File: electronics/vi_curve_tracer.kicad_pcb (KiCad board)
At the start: 2 copper layers, 60 x 37 mm, 65 parts, among them P1 CONN_01X05, P2 USB_OTG, P3 CONN_01X06, P4 CONN_01X06, P5 CONN_01X02, U1 MCP6004, U2 pic24f08km202, U3 ft230x

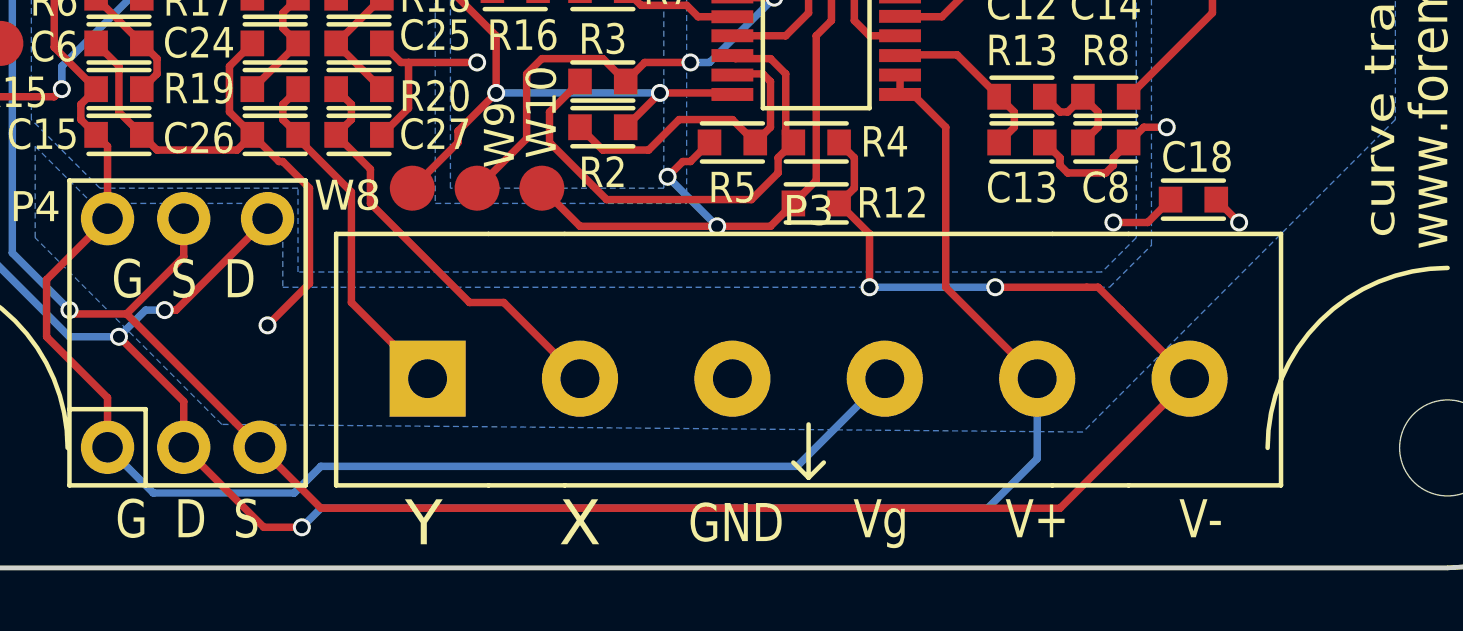
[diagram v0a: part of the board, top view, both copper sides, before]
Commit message: Slight adjustment of component placement
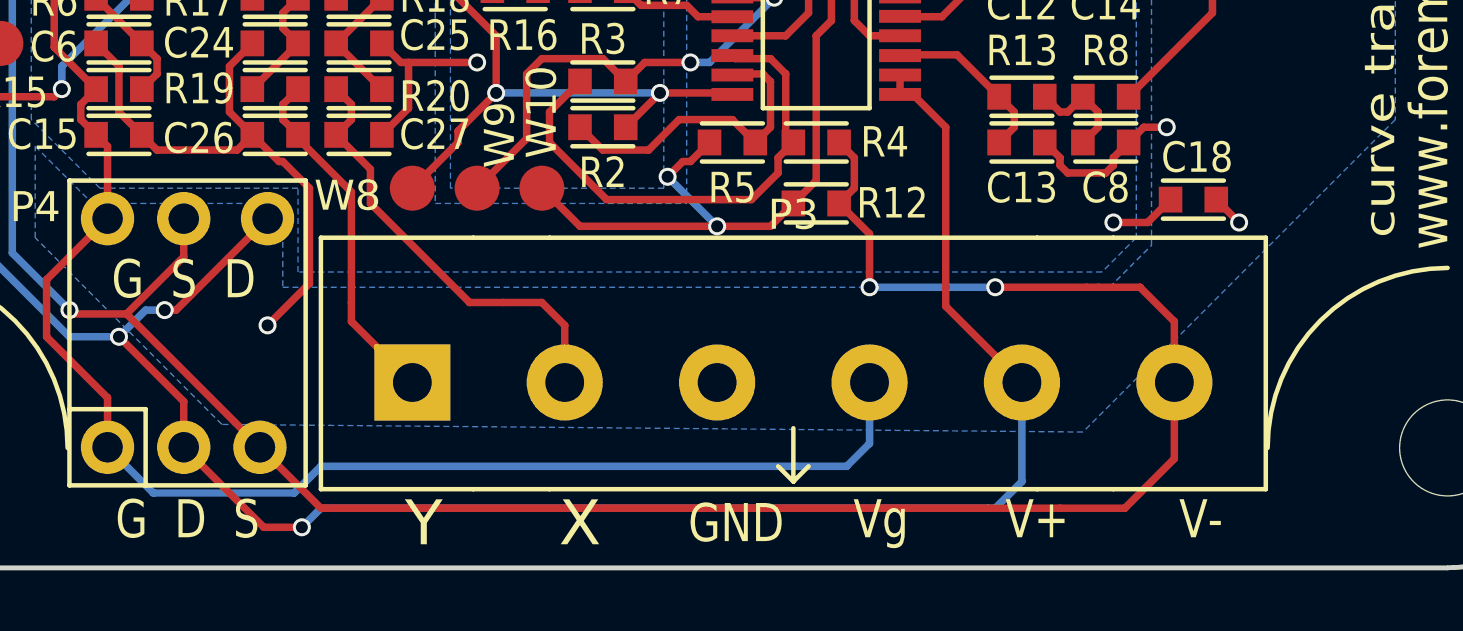
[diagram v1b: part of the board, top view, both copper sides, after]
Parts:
- moved P3 0.52 mm to (200.7, 106.0)
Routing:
- net LD_VOLTAGE_1: track 92.1 -> 93.8 mm
- net /x: track 14.1 -> 14.8 mm
- net GateVoltage: track 53.9 -> 54.5 mm
